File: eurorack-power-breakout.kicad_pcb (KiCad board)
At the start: 2 copper layers, 22.9 x 54.6 mm, 24 parts, among them J1 upper, J2 lower, J3 bus, J4 PWR, SW1 SW_SPDT

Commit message: :bookmark: Update the revision tag
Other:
- board text added: "v1.1"
- board text removed: "v1"
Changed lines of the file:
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@@
   (title_block
     (title "Eurorack Power Breakout")
-    (date "2023-01-06")
-    (rev "v1")
+    (date "2023-01-13")
+    (rev "1.1")
     (company "moPsy")
   )
@@
   (gr_line (start 127 90.17) (end 127 129.54) (layer "Edge.Cuts") (width 0.1))
   (gr_line (start 149.352 113.538) (end 149.098 113.792) (layer "Edge.Cuts") (width 0.1))
-  (gr_text "v1" (at 136.525 135.255 90) (layer "B.SilkS")
-    (effects (font (size 0.8 0.8) (thickness 0.1)) (justify mirror))
-  )
-  (gr_text "https://github.com/moPsy-project/eurorack-power-breakout" (at 134.62 116.84 90) (layer "B.SilkS")
-    (effects (font (size 0.8 0.8) (thickness 0.1)) (justify mirror))
+  (gr_text "v1.1" (at 136.398 134.874 90) (layer "B.SilkS")
+    (effects (font (size 0.8 0.8) (thickness 0.1)) (justify right mirror))
+  )
+  (gr_text "https://github.com/moPsy-project/eurorack-power-breakout" (at 134.62 134.62 90) (layer "B.SilkS")
+    (effects (font (size 0.8 0.8) (thickness 0.1)) (justify right mirror))
   )
   (gr_text "CC BY-SA 4.0\nStefan Haun" (at 145.288 119.507 90) (layer "B.SilkS")

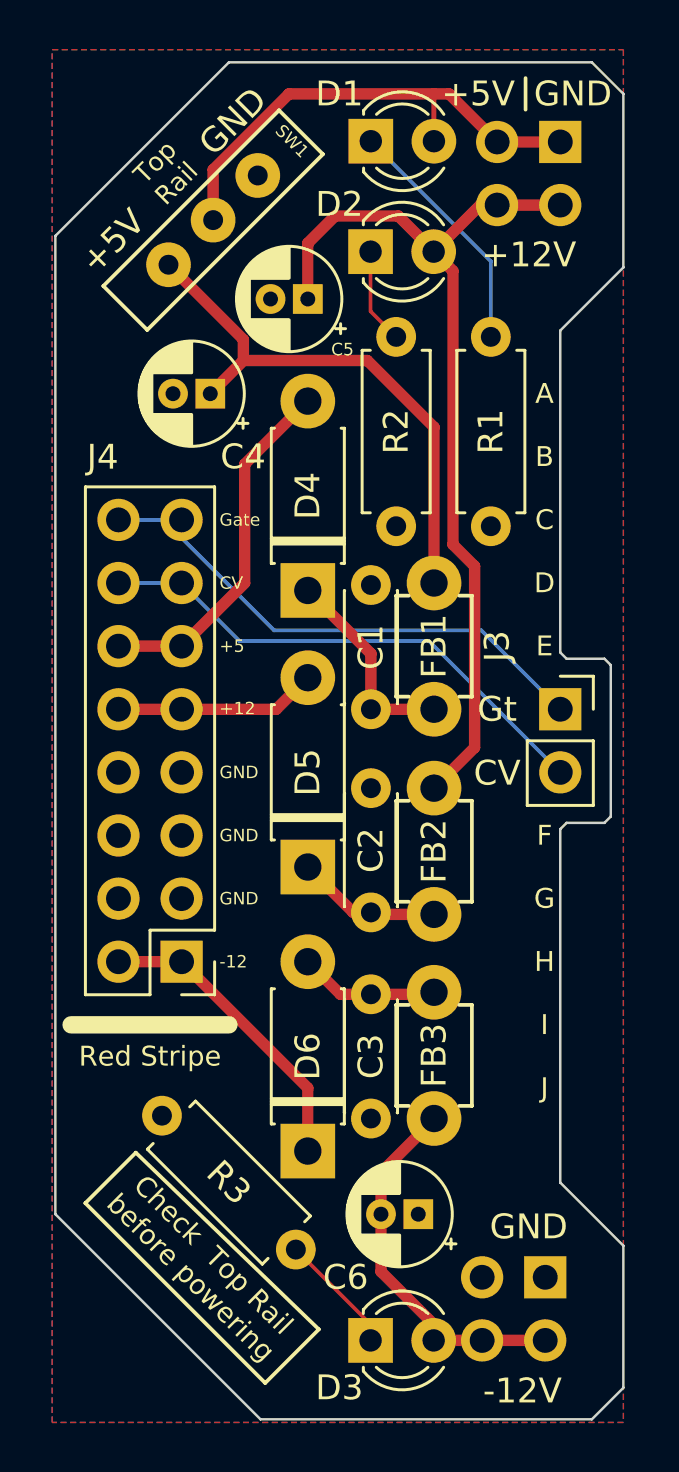
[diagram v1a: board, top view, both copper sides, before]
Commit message: :bug: Fix connector positioning and adjust dimensions
Fix posistions according to https://www.pololu.com/product/4000
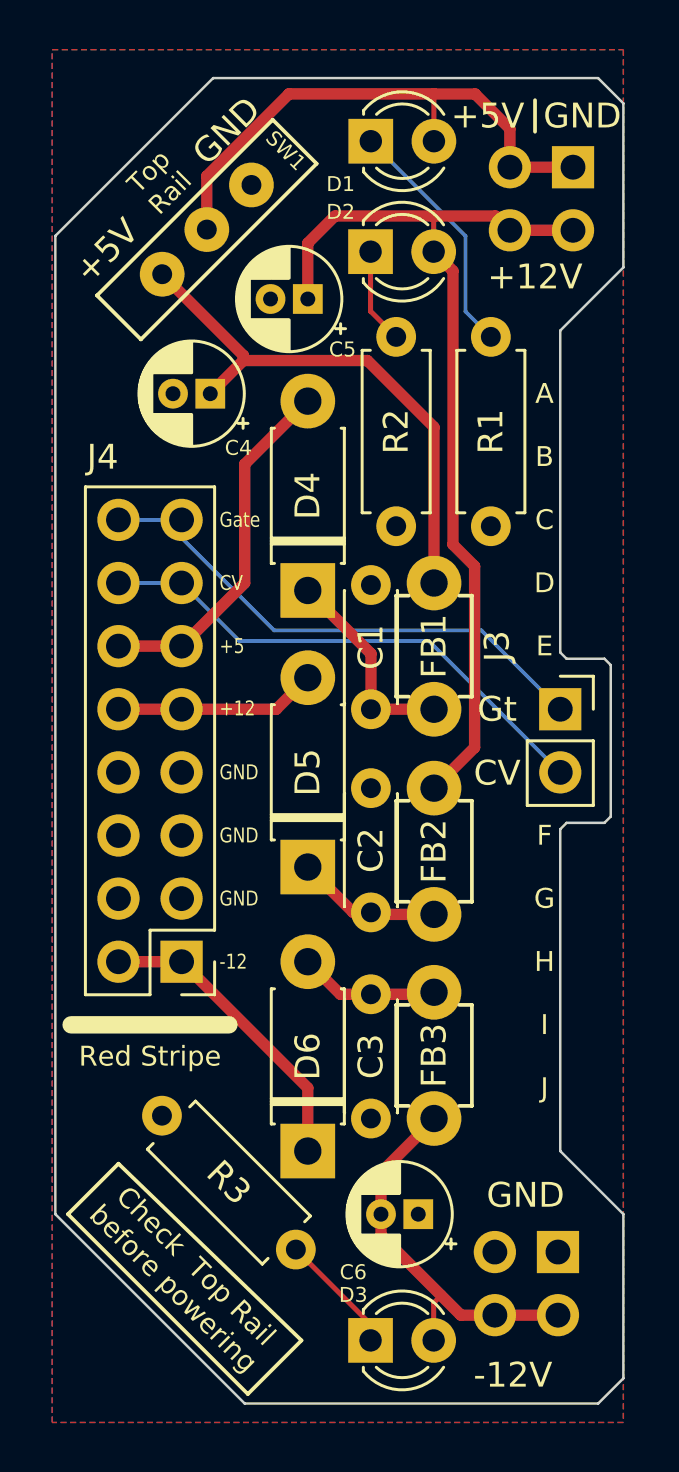
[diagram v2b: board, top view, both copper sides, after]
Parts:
- moved J2 1.14 mm to (147.2, 131.1)
- moved J1 1.14 mm to (147.8, 87.4)
- moved REF** 0.46 mm to (131.1, 91.9)
- moved SW1 0.46 mm to (133.1, 89.9)
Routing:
- net 5Vselect: track 20.0 -> 22.3 mm
- net +12V: track 37.2 -> 38.0 mm
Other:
- board size 22.9 x 54.6 mm -> 22.9 x 53.3 mm

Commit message: :bug: Adjust positions based on printouts
Even the pololou model was not perfect, adjust by another 0.005"

Fixes: #4
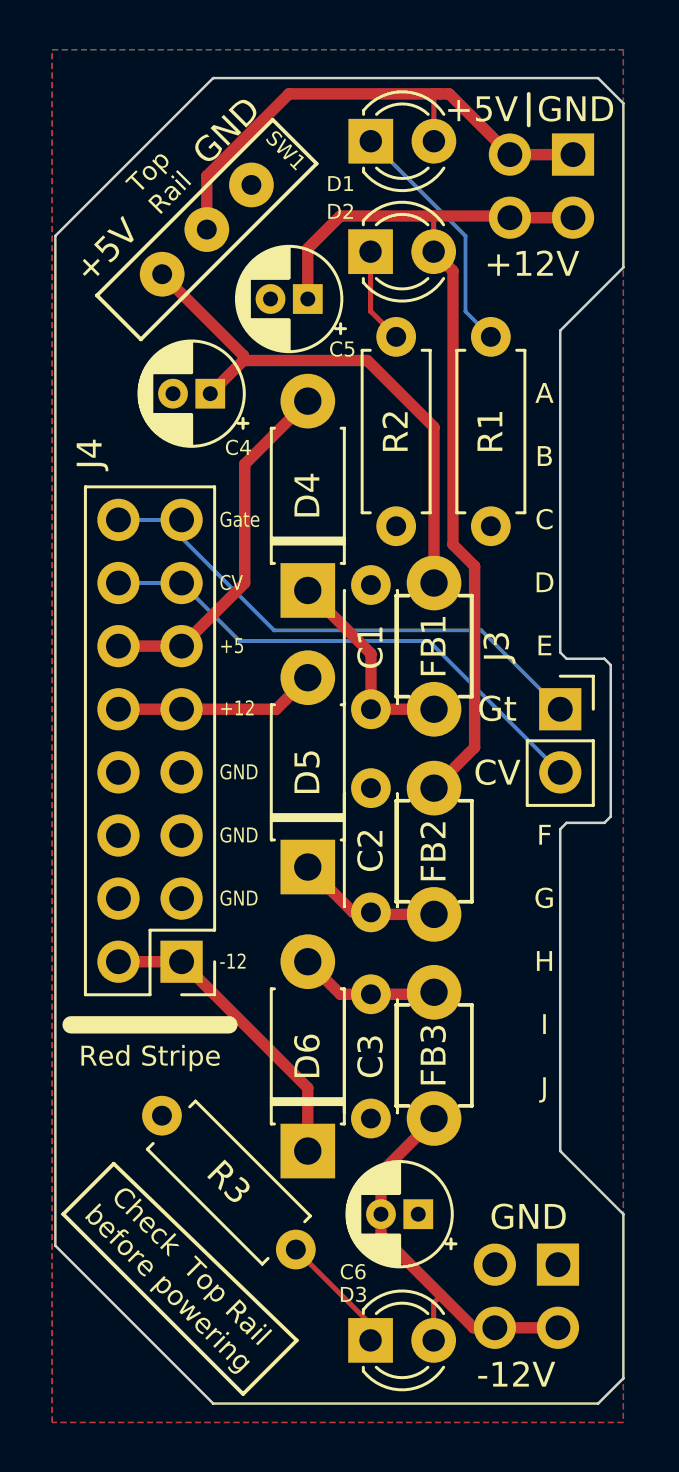
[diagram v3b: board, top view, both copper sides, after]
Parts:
- moved J1 0.51 mm to (147.8, 86.9)
- moved J2 0.51 mm to (147.2, 131.6)
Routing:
- net 5Vselect: track 22.3 -> 21.2 mm
- net -12V: track 15.5 -> 16.2 mm
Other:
- outline, holes or cut-outs redrawn
